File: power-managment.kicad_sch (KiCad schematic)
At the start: 0 parts

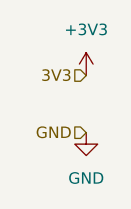
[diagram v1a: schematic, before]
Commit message: Updated heiarchal power labels
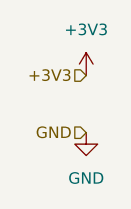
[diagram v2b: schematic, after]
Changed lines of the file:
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@@
 		(comment 1 "Ruhmit Sahu")
 	)
-	(hierarchical_label "3V3"
+	(hierarchical_label "+3V3"
 		(shape input)
 		(at 38.1 38.1 180)

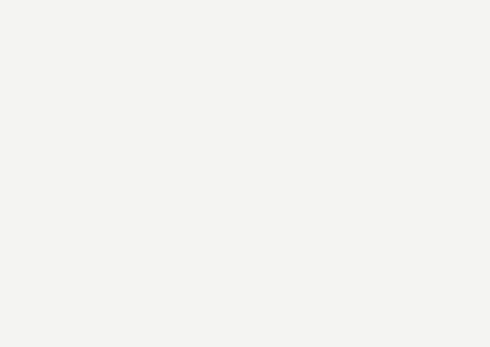
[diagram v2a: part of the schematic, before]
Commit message: Add battery for git testing
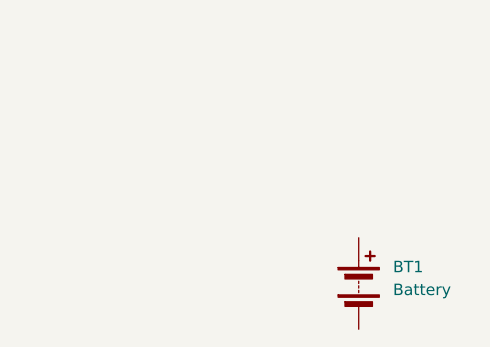
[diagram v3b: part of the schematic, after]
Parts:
- added BT1: Battery, symbol Device:Battery
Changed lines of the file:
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@@
 		(dnp no)
 		(fields_autoplaced yes)
-		(property "Reference" "#PWR042"
+		(property "Reference" "#PWR0101"
 			(at 38.1 50.8 0)
 			(effects
@@
 				(path "/2c2eadf0-5503-4531-8753-1a232087fe8c/ff86f43e-2806-4661-a460-b8d13650ca02"
 					(reference "#PWR042")
+					(unit 1)
+				)
+			)
+			(project "power-managment"
+				(path "/4a897c16-693b-45fb-822c-5a4e67f889c4"
+					(reference "#PWR0101")
 					(unit 1)
 				)
@@
 		(dnp no)
 		(fields_autoplaced yes)
-		(property "Reference" "#PWR041"
+		(property "Reference" "#PWR0102"
 			(at 38.1 41.91 0)
 			(effects
@@
 				)
 			)
-		)
-	)
+			(project "power-managment"
+				(path "/4a897c16-693b-45fb-822c-5a4e67f889c4"
+					(reference "#PWR0102")
+					(unit 1)
+				)
+			)
+		)
+	)
+	(symbol
+		(lib_id "Device:Battery")
+		(at 83.82 71.12 0)
+		(unit 1)
+		(exclude_from_sim no)
+		(in_bom yes)
+		(on_board no)
+		(dnp no)
+		(fields_autoplaced yes)
+		(property "Reference" "BT1"
+			(at 87.63 69.2784 0)
+			(effects
+				(font
+					(size 1.27 1.27)
+				)
+				(justify left)
+			)
+		)
+		(property "Value" "Battery"
+			(at 87.63 71.8184 0)
+			(effects
+				(font
+					(size 1.27 1.27)
+				)
+				(justify left)
+			)
+		)
+		(property "Footprint" ""
+			(at 83.82 69.596 90)
+			(effects
+				(font
+					(size 1.27 1.27)
+				)
+				(hide yes)
+			)
+		)
+		(property "Datasheet" "~"
+			(at 83.82 69.596 90)
+			(effects
+				(font
+					(size 1.27 1.27)
+				)
+				(hide yes)
+			)
+		)
+		(property "Description" "Multiple-cell battery"
+			(at 83.82 71.12 0)
+			(effects
+				(font
+					(size 1.27 1.27)
+				)
+				(hide yes)
+			)
+		)
+		(property "Sim.Device" "V"
+			(at 83.82 71.12 0)
+			(effects
+				(font
+					(size 1.27 1.27)
+				)
+				(hide yes)
+			)
+		)
+		(property "Sim.Type" "DC"
+			(at 83.82 71.12 0)
+			(effects
+				(font
+					(size 1.27 1.27)
+				)
+				(hide yes)
+			)
+		)
+		(property "Sim.Pins" "1=+ 2=-"
+			(at 83.82 71.12 0)
+			(effects
+				(font
+					(size 1.27 1.27)
+				)
+				(hide yes)
+			)
+		)
+		(pin "2"
+		)
+		(pin "1"
+		)
+		(instances
+			(project ""
+				(path "/4a897c16-693b-45fb-822c-5a4e67f889c4"
+					(reference "BT1")
+					(unit 1)
+				)
+			)
+		)
+	)
+	(sheet_instances
+		(path "/"
+			(page "1")
+		)
+	)
+	(embedded_fonts no)
 )

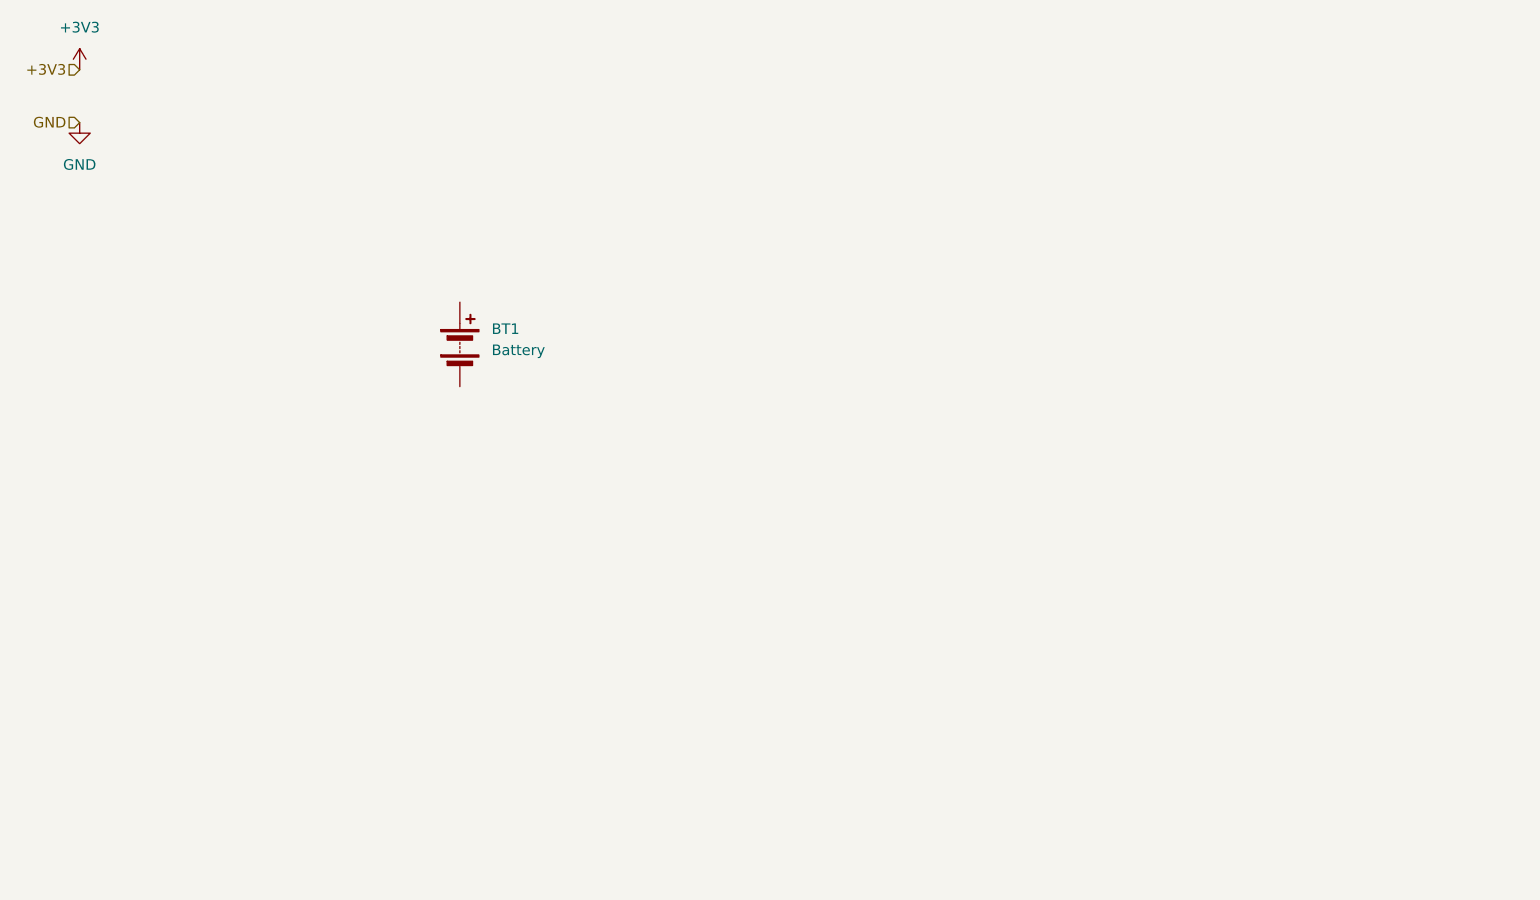
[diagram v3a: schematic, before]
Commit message: MPM3610 Power Buck Added
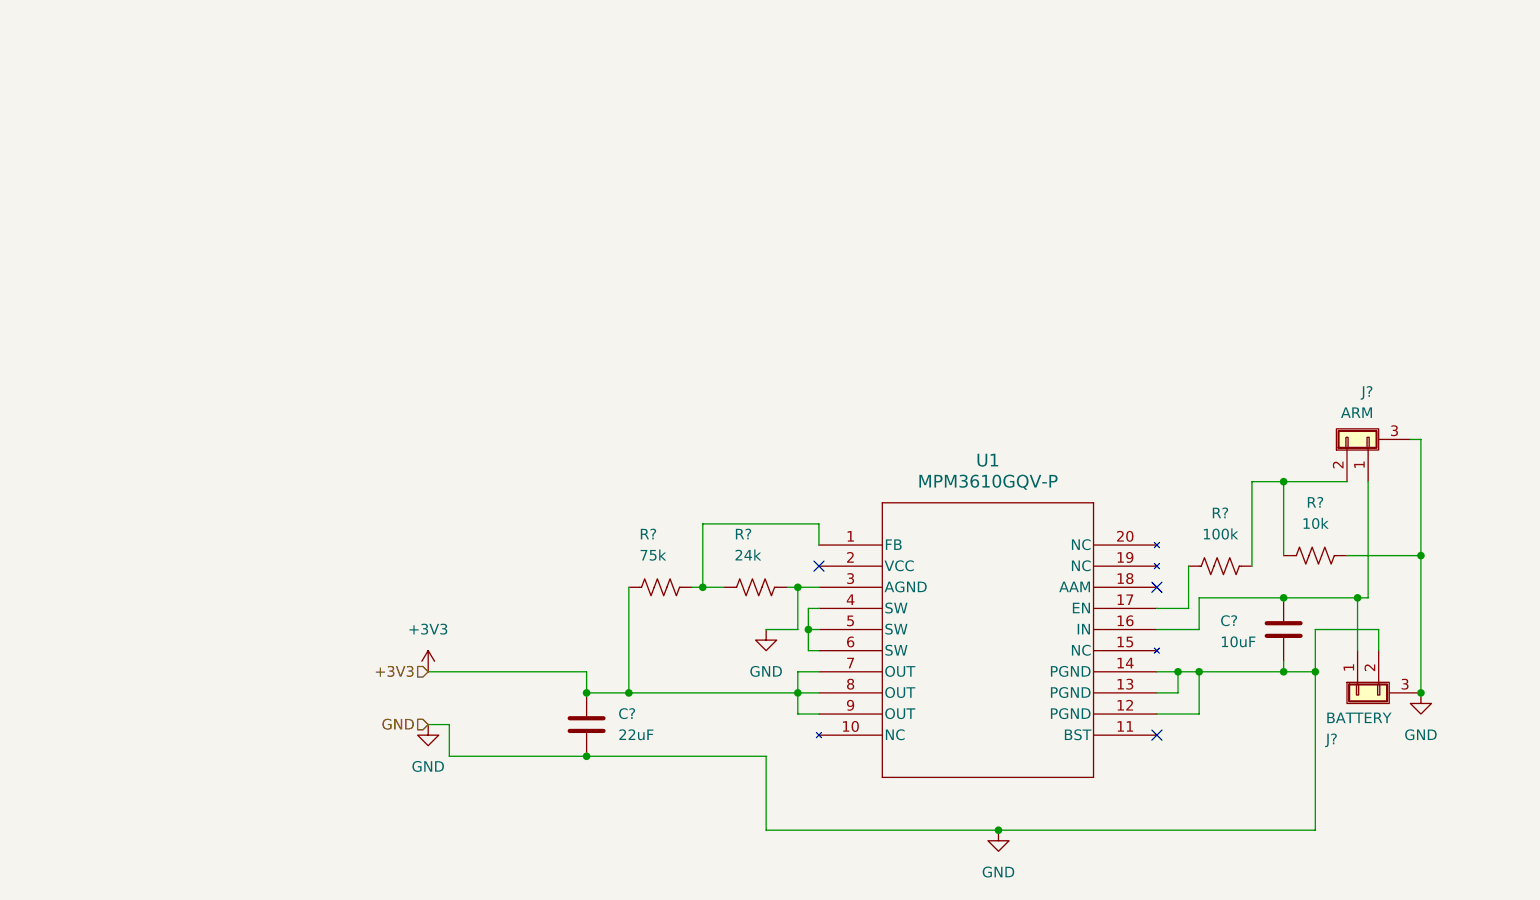
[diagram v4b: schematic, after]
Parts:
- removed BT1: Battery, symbol Device:Battery
- added C?: 10uF, symbol Device:C
- added C?: 22uF, symbol Device:C
- added J?: BATTERY, Avionics_Feet:0436500205, symbol Connector_Generic_Shielded:Conn_01x02_Shielded
- added J?: ARM, Avionics_Feet:0436500205, symbol Connector_Generic_Shielded:Conn_01x02_Shielded
- added R?: 10k, symbol Device:R_US
- added R?: 100k, symbol Device:R_US
- added R?: 24k, symbol Device:R_US
- added R?: 75k, symbol Device:R_US
- added U1: MPM3610GQV-P, symbol Avionics_Symbols:MPM3610GQV-P
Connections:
- net +3V3: now also C?.1, R?.1, U1.7 (OUT), U1.8 (OUT), U1.9 (OUT)
- net GND: now also C?.2, C?.2, J?.2 (Pin_2), J?.3 (Shield), J?.3 (Shield), R?.2, R?.2, U1.12 (PGND), U1.13 (PGND), U1.14 (PGND), U1.3 (AGND)
- new net: C?.1, J?.1 (Pin_1), J?.1 (Pin_2), U1.16 (IN)
- new net: J?.2 (Pin_1), R?.1, R?.2
- new net: R?.1, R?.2, U1.1 (FB)
- new net: R?.1, U1.17 (EN)
- new net: U1.4 (SW), U1.5 (SW), U1.6 (SW)
- no-connect marks 0 -> 3

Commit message: Julia cleaning wires
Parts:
- removed C?: 10uF, symbol Device:C
- removed J?: BATTERY, Avionics_Feet:0436500205, symbol Connector_Generic_Shielded:Conn_01x02_Shielded
- added C1: 20uF, symbol Device:C_Small
- added J1: BATTERY, Avionics_Feet:0436500205, symbol Connector_Generic_Shielded:Conn_01x02_Shielded
- gave numbers to parts that had none: 6
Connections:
- net GND: now also C1.2, J1.2 (Pin_2), J1.3 (Shield)
- net at J2.1 (Pin_2), U1.16 (IN): now also C1.1, J1.1 (Pin_1)
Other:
- moved on the sheet: C2, J2, R1, R4

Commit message: Update resistors
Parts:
- removed R3: 100k, symbol Device:R_US
- added R4: 39k, symbol Device:R_US
- C1: value 20uF -> 10uF
- renumbered R4 to R3
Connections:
- net GND: now also R4.2
- net at J2.2 (Pin_1), R3.1: now also U1.17 (EN)
- net at U1.18 (AAM): now also R4.1
- no-connect marks 3 -> 2
